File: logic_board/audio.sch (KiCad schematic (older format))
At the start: 20 parts, among them J2 Audio In, J3 SJ2-3595X-SMT, U2 OPA340NA, U3 WM8731SEDS_V, Y2 12MHz

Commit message: Re-layout for the third time
In general, tried to make things a bit cleaner. Also:
- Needed to add a capacitor on charger output.
- Use a footprint with copper pad under charger for heat dissipation
- Use through-hole LEDs, which are easier to bend 90 degrees to poke out
  the sides of the case.
- I read about a trick: put all power supply bypass caps under the IC, which
  saves space.
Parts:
- added C10: 0.1uF, Capacitors_SMD:C_0402, symbol Device:C
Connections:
- net +3V3: now also C10.1
- net GND: now also C10.2
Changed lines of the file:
@@
 Wire Wire Line
 	3450 3550 3450 3500
+$Comp
+L Device:C C10
+U 1 1 5E3526BE
+P 5050 6450
+F 0 "C10" H 5165 6496 50  0000 L CNN
+F 1 "0.1uF" H 5165 6405 50  0000 L CNN
+F 2 "Capacitors_SMD:C_0402" H 5088 6300 50  0001 C CNN
+F 3 "~" H 5050 6450 50  0001 C CNN
+	1    5050 6450
+	1    0    0    -1
+$EndComp
+Wire Wire Line
+	4650 6050 5050 6050
+Wire Wire Line
+	5050 6050 5050 6300
+Connection ~ 4650 6050
+Wire Wire Line
+	4650 6850 5050 6850
+Wire Wire Line
+	5050 6850 5050 6600
+Connection ~ 4650 6850
 $EndSCHEMATC

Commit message: Update BOM
Move power/charge LEDs back from edge so there's enough room. Use horizontal footprint.
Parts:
- C12: value 0.1 uF -> 0.1uF
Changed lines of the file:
@@
 P 2650 3950
 F 0 "C12" V 2398 3950 50  0000 C CNN
-F 1 "0.1 uF" V 2489 3950 50  0000 C CNN
+F 1 "0.1uF" V 2489 3950 50  0000 C CNN
 F 2 "Capacitors_SMD:C_0402" H 2688 3800 50  0001 C CNN
 F 3 "~" H 2650 3950 50  0001 C CNN

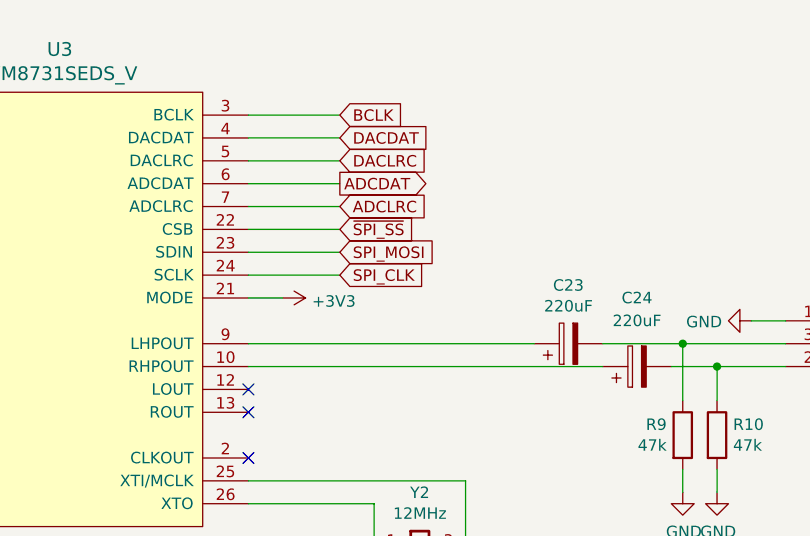
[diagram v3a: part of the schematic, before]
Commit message: Switch to a microcontroller with more SRAM
This is necessary to enable some effects like reverb and echo.
This part has a similar pinout, but not exactly the same, which required some layout
changes.
I also took this opportuntity to move the serial pins to a separate header with its
own ground, which makes connecting a serial debugger and SWD interface at the same
time easier.
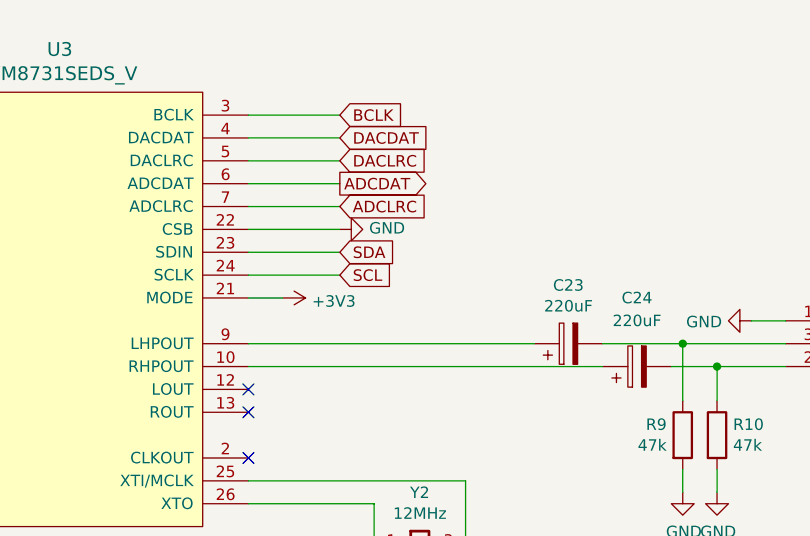
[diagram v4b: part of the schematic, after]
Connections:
- net ~SPI_SS is gone; now on net GND: U3.22 (CSB)
- net SPI_CLK renamed SCL
- net SPI_MOSI renamed SDA
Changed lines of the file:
@@
 Sheet 3 4
 Title "Audio"
-Date "2020-02-02"
-Rev "1.0"
+Date "2020-02-08"
+Rev "1.1"
 Comp ""
 Comment1 ""
@@
 	6650 2650 7050 2650
 Text GLabel 7050 2850 2    50   Input ~ 0
-SPI_MOSI
+SDA
 Text GLabel 7050 2950 2    50   Input ~ 0
-SPI_CLK
+SCL
 Wire Wire Line
 	6650 2850 7050 2850
@@
 	0    1    1    0
 $EndComp
-Text GLabel 7050 2750 2    50   Input ~ 0
-~SPI_SS
 Wire Wire Line
 	6650 2750 7050 2750
@@
 	5050 6850 5050 6600
 Connection ~ 4650 6850
+$Comp
+L power:GND #PWR0104
+U 1 1 5E56A195
+P 7050 2750
+F 0 "#PWR0104" H 7050 2500 50  0001 C CNN
+F 1 "GND" V 7055 2622 50  0000 R CNN
+F 2 "" H 7050 2750 50  0001 C CNN
+F 3 "" H 7050 2750 50  0001 C CNN
+	1    7050 2750
+	0    -1   -1   0
+$EndComp
 $EndSCHEMATC

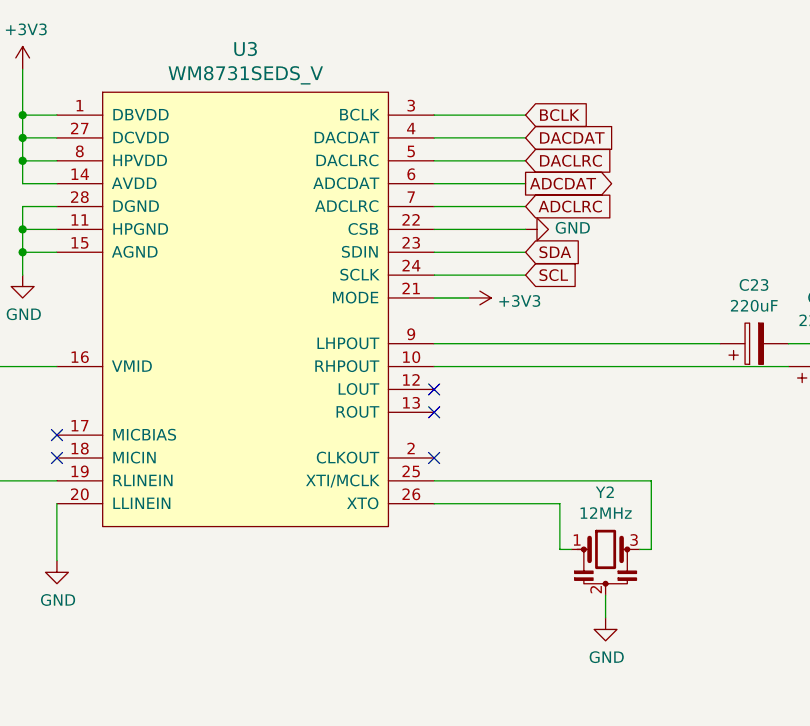
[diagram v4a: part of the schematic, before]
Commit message: Fix a few incorrect MCU pin connections from last change.
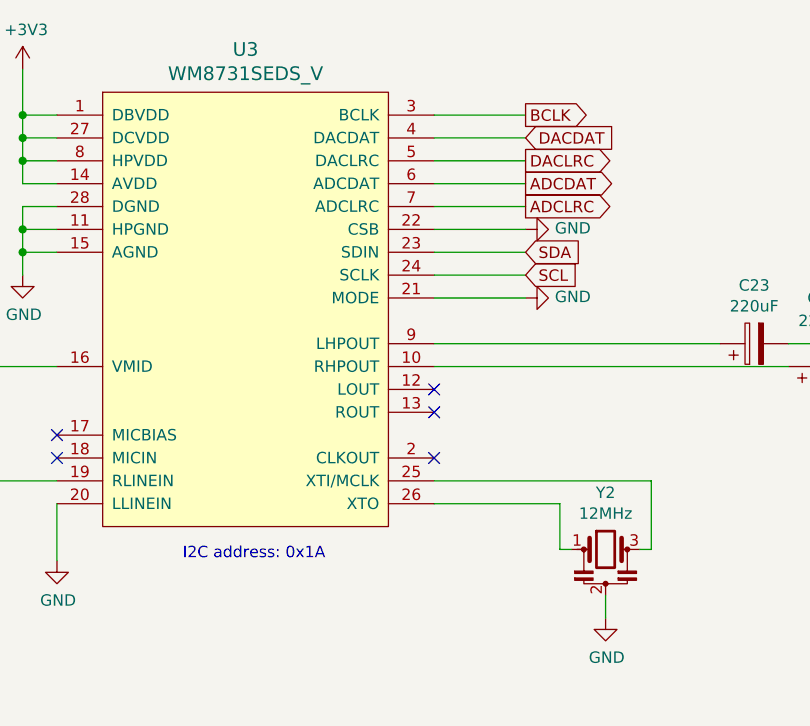
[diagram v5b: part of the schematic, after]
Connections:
- net +3V3: no longer U3.21 (MODE)
- net GND: now also U3.21 (MODE)
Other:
- note added: "I2C address: 0x1A"
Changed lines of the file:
@@
 Wire Wire Line
 	8700 3350 9000 3350
-Text GLabel 7050 2250 2    50   Input ~ 0
+Text GLabel 7050 2250 2    50   Output ~ 0
 BCLK
 Text GLabel 7050 2350 2    50   Input ~ 0
 DACDAT
-Text GLabel 7050 2450 2    50   Input ~ 0
+Text GLabel 7050 2450 2    50   Output ~ 0
 DACLRC
 Text GLabel 7050 2550 2    50   Output ~ 0
 ADCDAT
-Text GLabel 7050 2650 2    50   Input ~ 0
+Text GLabel 7050 2650 2    50   Output ~ 0
 ADCLRC
 Wire Wire Line
@@
 Wire Wire Line
 	6650 2950 7050 2950
-Wire Wire Line
-	6650 3050 6800 3050
 $Comp
 L power:GND #PWR020
@@
 	1    3450 3500
 	1    0    0    -1
-$EndComp
-$Comp
-L power:+3V3 #PWR022
-U 1 1 5E2E70D7
-P 6800 3050
-F 0 "#PWR022" H 6800 2900 50  0001 C CNN
-F 1 "+3V3" V 6815 3178 50  0000 L CNN
-F 2 "" H 6800 3050 50  0001 C CNN
-F 3 "" H 6800 3050 50  0001 C CNN
-	1    6800 3050
-	0    1    1    0
 $EndComp
 Wire Wire Line
@@
 	0    -1   -1   0
 $EndComp
+$Comp
+L power:GND #PWR0107
+U 1 1 5E3FC3F1
+P 7050 3050
+F 0 "#PWR0107" H 7050 2800 50  0001 C CNN
+F 1 "GND" V 7055 2922 50  0000 R CNN
+F 2 "" H 7050 3050 50  0001 C CNN
+F 3 "" H 7050 3050 50  0001 C CNN
+	1    7050 3050
+	0    -1   -1   0
+$EndComp
+Wire Wire Line
+	6650 3050 7050 3050
+Text Notes 5550 4200 0    50   ~ 0
+I2C address: 0x1A
 $EndSCHEMATC

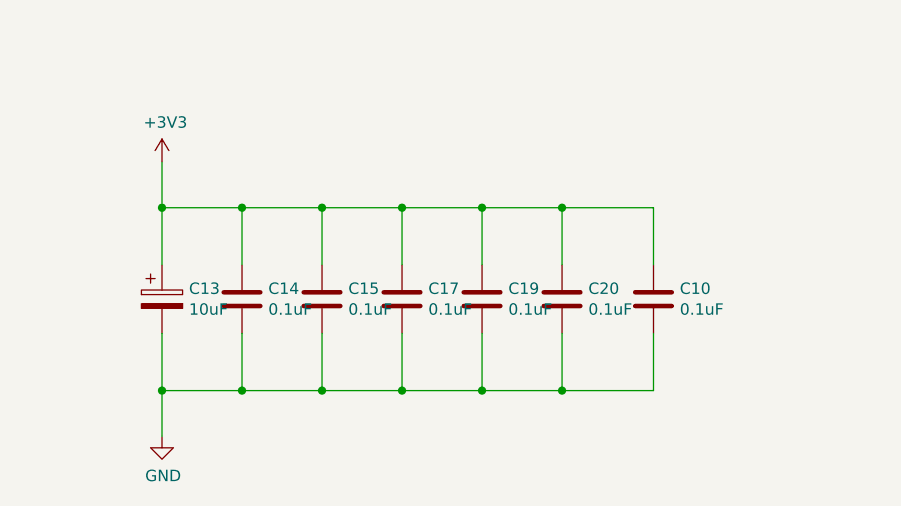
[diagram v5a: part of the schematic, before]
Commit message: PCB layout cleanup
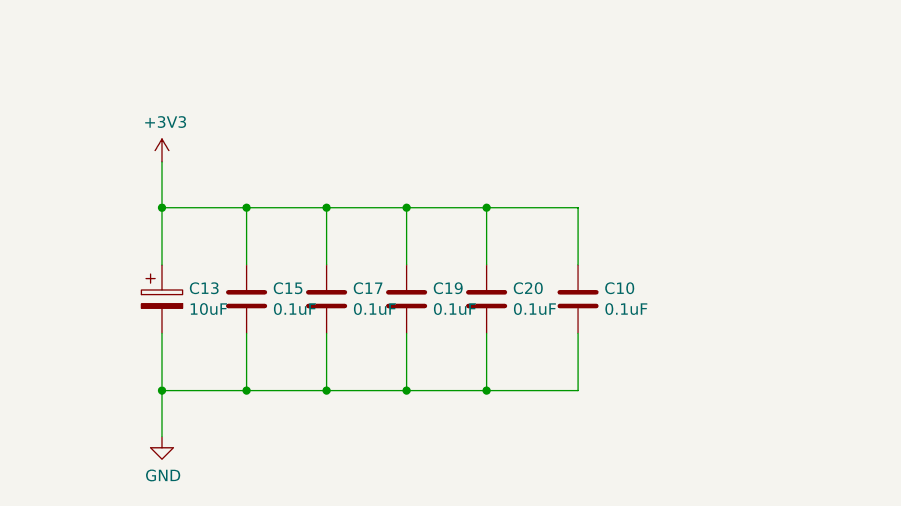
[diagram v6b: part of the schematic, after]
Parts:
- removed C14: 0.1uF, Capacitors_SMD:C_0402, symbol Device:C
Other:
- moved on the sheet: C10, C15, C17, C19, C20
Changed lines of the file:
@@
 L Device:C C15
 U 1 1 5E313624
-P 3600 6450
-F 0 "C15" H 3715 6496 50  0000 L CNN
-F 1 "0.1uF" H 3715 6405 50  0000 L CNN
-F 2 "Capacitors_SMD:C_0402" H 3638 6300 50  0001 C CNN
-F 3 "~" H 3600 6450 50  0001 C CNN
-	1    3600 6450
+P 3270 6450
+F 0 "C15" H 3385 6496 50  0000 L CNN
+F 1 "0.1uF" H 3385 6405 50  0000 L CNN
+F 2 "Capacitors_SMD:C_0402" H 3308 6300 50  0001 C CNN
+F 3 "~" H 3270 6450 50  0001 C CNN
+	1    3270 6450
 	1    0    0    -1
 $EndComp
@@
 L Device:C C17
 U 1 1 5E313F61
-P 3950 6450
-F 0 "C17" H 4065 6496 50  0000 L CNN
-F 1 "0.1uF" H 4065 6405 50  0000 L CNN
-F 2 "Capacitors_SMD:C_0402" H 3988 6300 50  0001 C CNN
-F 3 "~" H 3950 6450 50  0001 C CNN
-	1    3950 6450
+P 3620 6450
+F 0 "C17" H 3735 6496 50  0000 L CNN
+F 1 "0.1uF" H 3735 6405 50  0000 L CNN
+F 2 "Capacitors_SMD:C_0402" H 3658 6300 50  0001 C CNN
+F 3 "~" H 3620 6450 50  0001 C CNN
+	1    3620 6450
 	1    0    0    -1
 $EndComp
@@
 L Device:C C19
 U 1 1 5E31490C
-P 4300 6450
-F 0 "C19" H 4415 6496 50  0000 L CNN
-F 1 "0.1uF" H 4415 6405 50  0000 L CNN
-F 2 "Capacitors_SMD:C_0402" H 4338 6300 50  0001 C CNN
-F 3 "~" H 4300 6450 50  0001 C CNN
-	1    4300 6450
-	1    0    0    -1
-$EndComp
-Wire Wire Line
-	4300 6050 4300 6300
-Wire Wire Line
-	2900 6300 2900 6050
-Connection ~ 2900 6050
-Wire Wire Line
-	2900 6050 3250 6050
-Wire Wire Line
-	3250 6300 3250 6050
-Connection ~ 3250 6050
-Wire Wire Line
-	3250 6050 3600 6050
-Wire Wire Line
-	3600 6300 3600 6050
-Connection ~ 3600 6050
-Wire Wire Line
-	3600 6050 3950 6050
-Wire Wire Line
-	3950 6300 3950 6050
-Connection ~ 3950 6050
-Wire Wire Line
-	3950 6050 4300 6050
-Wire Wire Line
-	4300 6850 4300 6600
-Wire Wire Line
-	2900 6600 2900 6850
-Connection ~ 2900 6850
-Wire Wire Line
-	2900 6850 3250 6850
-Wire Wire Line
-	3250 6600 3250 6850
-Connection ~ 3250 6850
-Wire Wire Line
-	3250 6850 3600 6850
-Wire Wire Line
-	3600 6600 3600 6850
-Connection ~ 3600 6850
-Wire Wire Line
-	3600 6850 3950 6850
-Wire Wire Line
-	3950 6600 3950 6850
-Connection ~ 3950 6850
-Wire Wire Line
-	3950 6850 4300 6850
+P 3970 6450
+F 0 "C19" H 4085 6496 50  0000 L CNN
+F 1 "0.1uF" H 4085 6405 50  0000 L CNN
+F 2 "Capacitors_SMD:C_0402" H 4008 6300 50  0001 C CNN
+F 3 "~" H 3970 6450 50  0001 C CNN
+	1    3970 6450
+	1    0    0    -1
+$EndComp
+Wire Wire Line
+	3970 6050 3970 6300
+Wire Wire Line
+	3270 6300 3270 6050
+Wire Wire Line
+	3270 6050 3620 6050
+Wire Wire Line
+	3620 6300 3620 6050
+Connection ~ 3620 6050
+Wire Wire Line
+	3620 6050 3970 6050
+Wire Wire Line
+	3970 6850 3970 6600
+Wire Wire Line
+	3270 6600 3270 6850
+Wire Wire Line
+	3270 6850 3620 6850
+Wire Wire Line
+	3620 6600 3620 6850
+Connection ~ 3620 6850
+Wire Wire Line
+	3620 6850 3970 6850
 $Comp
 L power:+3V3 #PWR013
@@
 	1    0    0    -1
 $EndComp
-Wire Wire Line
-	2900 6050 2900 5850
-Wire Wire Line
-	2900 7050 2900 6850
-$Comp
-L Device:C C14
-U 1 1 5E313104
-P 3250 6450
-F 0 "C14" H 3365 6496 50  0000 L CNN
-F 1 "0.1uF" H 3365 6405 50  0000 L CNN
-F 2 "Capacitors_SMD:C_0402" H 3288 6300 50  0001 C CNN
-F 3 "~" H 3250 6450 50  0001 C CNN
-	1    3250 6450
-	1    0    0    -1
-$EndComp
 $Comp
 L Device:CP C13
@@
 L Device:C C20
 U 1 1 5E51D0FC
-P 4650 6450
-F 0 "C20" H 4765 6496 50  0000 L CNN
-F 1 "0.1uF" H 4765 6405 50  0000 L CNN
-F 2 "Capacitors_SMD:C_0402" H 4688 6300 50  0001 C CNN
-F 3 "~" H 4650 6450 50  0001 C CNN
-	1    4650 6450
-	1    0    0    -1
-$EndComp
-Wire Wire Line
-	4300 6050 4650 6050
-Wire Wire Line
-	4650 6050 4650 6300
-Connection ~ 4300 6050
-Wire Wire Line
-	4300 6850 4650 6850
-Wire Wire Line
-	4650 6850 4650 6600
-Connection ~ 4300 6850
+P 4320 6450
+F 0 "C20" H 4435 6496 50  0000 L CNN
+F 1 "0.1uF" H 4435 6405 50  0000 L CNN
+F 2 "Capacitors_SMD:C_0402" H 4358 6300 50  0001 C CNN
+F 3 "~" H 4320 6450 50  0001 C CNN
+	1    4320 6450
+	1    0    0    -1
+$EndComp
+Wire Wire Line
+	3970 6050 4320 6050
+Wire Wire Line
+	4320 6050 4320 6300
+Connection ~ 3970 6050
+Wire Wire Line
+	3970 6850 4320 6850
+Wire Wire Line
+	4320 6850 4320 6600
+Connection ~ 3970 6850
 $Comp
 L Device:CP C23
@@
 L Device:C C10
 U 1 1 5E3526BE
-P 5050 6450
-F 0 "C10" H 5165 6496 50  0000 L CNN
-F 1 "0.1uF" H 5165 6405 50  0000 L CNN
-F 2 "Capacitors_SMD:C_0402" H 5088 6300 50  0001 C CNN
-F 3 "~" H 5050 6450 50  0001 C CNN
-	1    5050 6450
-	1    0    0    -1
-$EndComp
-Wire Wire Line
-	4650 6050 5050 6050
-Wire Wire Line
-	5050 6050 5050 6300
-Connection ~ 4650 6050
-Wire Wire Line
-	4650 6850 5050 6850
-Wire Wire Line
-	5050 6850 5050 6600
-Connection ~ 4650 6850
+P 4720 6450
+F 0 "C10" H 4835 6496 50  0000 L CNN
+F 1 "0.1uF" H 4835 6405 50  0000 L CNN
+F 2 "Capacitors_SMD:C_0402" H 4758 6300 50  0001 C CNN
+F 3 "~" H 4720 6450 50  0001 C CNN
+	1    4720 6450
+	1    0    0    -1
+$EndComp
+Wire Wire Line
+	4320 6050 4720 6050
+Wire Wire Line
+	4720 6050 4720 6300
+Connection ~ 4320 6050
+Wire Wire Line
+	4320 6850 4720 6850
+Wire Wire Line
+	4720 6850 4720 6600
+Connection ~ 4320 6850
 $Comp
 L power:GND #PWR0104
@@
 Text Notes 5550 4200 0    50   ~ 0
 I2C address: 0x1A
+Wire Wire Line
+	2900 5850 2900 6050
+Wire Wire Line
+	2900 6600 2900 6850
+Wire Wire Line
+	3270 6050 2900 6050
+Connection ~ 3270 6050
+Connection ~ 2900 6050
+Wire Wire Line
+	2900 6050 2900 6300
+Wire Wire Line
+	3270 6850 2900 6850
+Connection ~ 3270 6850
+Connection ~ 2900 6850
+Wire Wire Line
+	2900 6850 2900 7050
 $EndSCHEMATC
